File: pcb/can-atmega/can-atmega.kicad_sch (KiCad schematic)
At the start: 27 parts, among them J1 Screw_Terminal_01x02, J2 Screw_Terminal_01x02, J3 Conn_01x04_Female, J4 Conn_01x02_Female, J5 Conn_01x08_Female, U1 LM1117-5.0, U2 TJA1051T, U3 MCP2515-xSO, U4 ATmega328P-A, X1 16MHz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

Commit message: motor module
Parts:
- removed J4: Conn_01x02_Female, Connector_PinSocket_2.54mm:PinSocket_1x02_P2.54mm_Vertical, symbol Connector:Conn_01x02_Female
- removed J5: Conn_01x08_Female, Connector_PinSocket_2.54mm:PinSocket_1x08_P2.54mm_Vertical, symbol Connector:Conn_01x08_Female
- added J4: Connector_female, CAN_ATmega:Connector_female, symbol CAN_ATmega:Connector_female
- C1, C10, C11, C12, C3, C4, C5, C6, C7, C9: footprint Capacitor_SMD_Custom:C_KEM_0805_2.0x1.25mm -> Capacitor_SMD:C_1206_3216Metric
- C2, C8: footprint Capacitor_SMD_Custom:C_TAJ_3516_Bauform_A -> Capacitor_SMD:C_1206_3216Metric
- LED1: footprint LED_SMD_Custom:LED_EL_0603_GR1_1608 -> LED_SMD:LED_0805_2012Metric
- R1, R2, R3: footprint Resistors_SMD_Custom:R_SPR-0603_1.6x0.8mm -> Resistor_SMD:R_0805_2012Metric
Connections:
- net +5V: now also J4.2 (+5V)
- net GND: now also J4.3 (GND)
- net U4_A0: now also J4.8 (A0)
- net U4_A1: now also J4.9 (A1)
- net U4_A2: now also J4.10 (A2)
- net U4_A3: now also J4.11 (A3)
- net U4_D3: now also J4.4 (D3)
- net U4_D4: now also J4.5 (D4)
- net U4_D5: now also J4.6 (D5)
- net U4_D6: now also J4.7 (D6)
- net 12V renamed +12V
- net +12V: now also J4.1 (+12V)

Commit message: update pcb
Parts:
- J1, J2: footprint TerminalBlock:TerminalBlock_bornier-2_P5.08mm -> TerminalBlock_Phoenix:TerminalBlock_Phoenix_MKDS-1,5-2-5.08_1x02_P5.08mm_Horizontal
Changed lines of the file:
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@@
       (effects (font (size 1.27 1.27)) (justify left) hide)
     )
-    (property "Footprint" "TerminalBlock:TerminalBlock_bornier-2_P5.08mm" (id 2) (at 276.86 34.29 0)
+    (property "Footprint" "TerminalBlock_Phoenix:TerminalBlock_Phoenix_MKDS-1,5-2-5.08_1x02_P5.08mm_Horizontal" (id 2) (at 276.86 34.29 0)
       (effects (font (size 1.27 1.27)) hide)
     )
@@
       (effects (font (size 1.27 1.27)) (justify left) hide)
     )
-    (property "Footprint" "TerminalBlock:TerminalBlock_bornier-2_P5.08mm" (id 2) (at 24.13 31.75 0)
+    (property "Footprint" "TerminalBlock_Phoenix:TerminalBlock_Phoenix_MKDS-1,5-2-5.08_1x02_P5.08mm_Horizontal" (id 2) (at 24.13 31.75 0)
       (effects (font (size 1.27 1.27)) hide)
     )
@@
     )
     (path "/71aba0ac-da00-46fc-b041-6f563b5b4142"
-      (reference "J1") (unit 1) (value "Screw_Terminal_01x02") (footprint "TerminalBlock:TerminalBlock_bornier-2_P5.08mm")
+      (reference "J1") (unit 1) (value "Screw_Terminal_01x02") (footprint "TerminalBlock_Phoenix:TerminalBlock_Phoenix_MKDS-1,5-2-5.08_1x02_P5.08mm_Horizontal")
     )
     (path "/2120f6af-caaf-4baf-8a36-50ada20126a7"
-      (reference "J2") (unit 1) (value "Screw_Terminal_01x02") (footprint "TerminalBlock:TerminalBlock_bornier-2_P5.08mm")
+      (reference "J2") (unit 1) (value "Screw_Terminal_01x02") (footprint "TerminalBlock_Phoenix:TerminalBlock_Phoenix_MKDS-1,5-2-5.08_1x02_P5.08mm_Horizontal")
     )
     (path "/1e97e435-8faf-41d7-b7b1-5859024e8060"

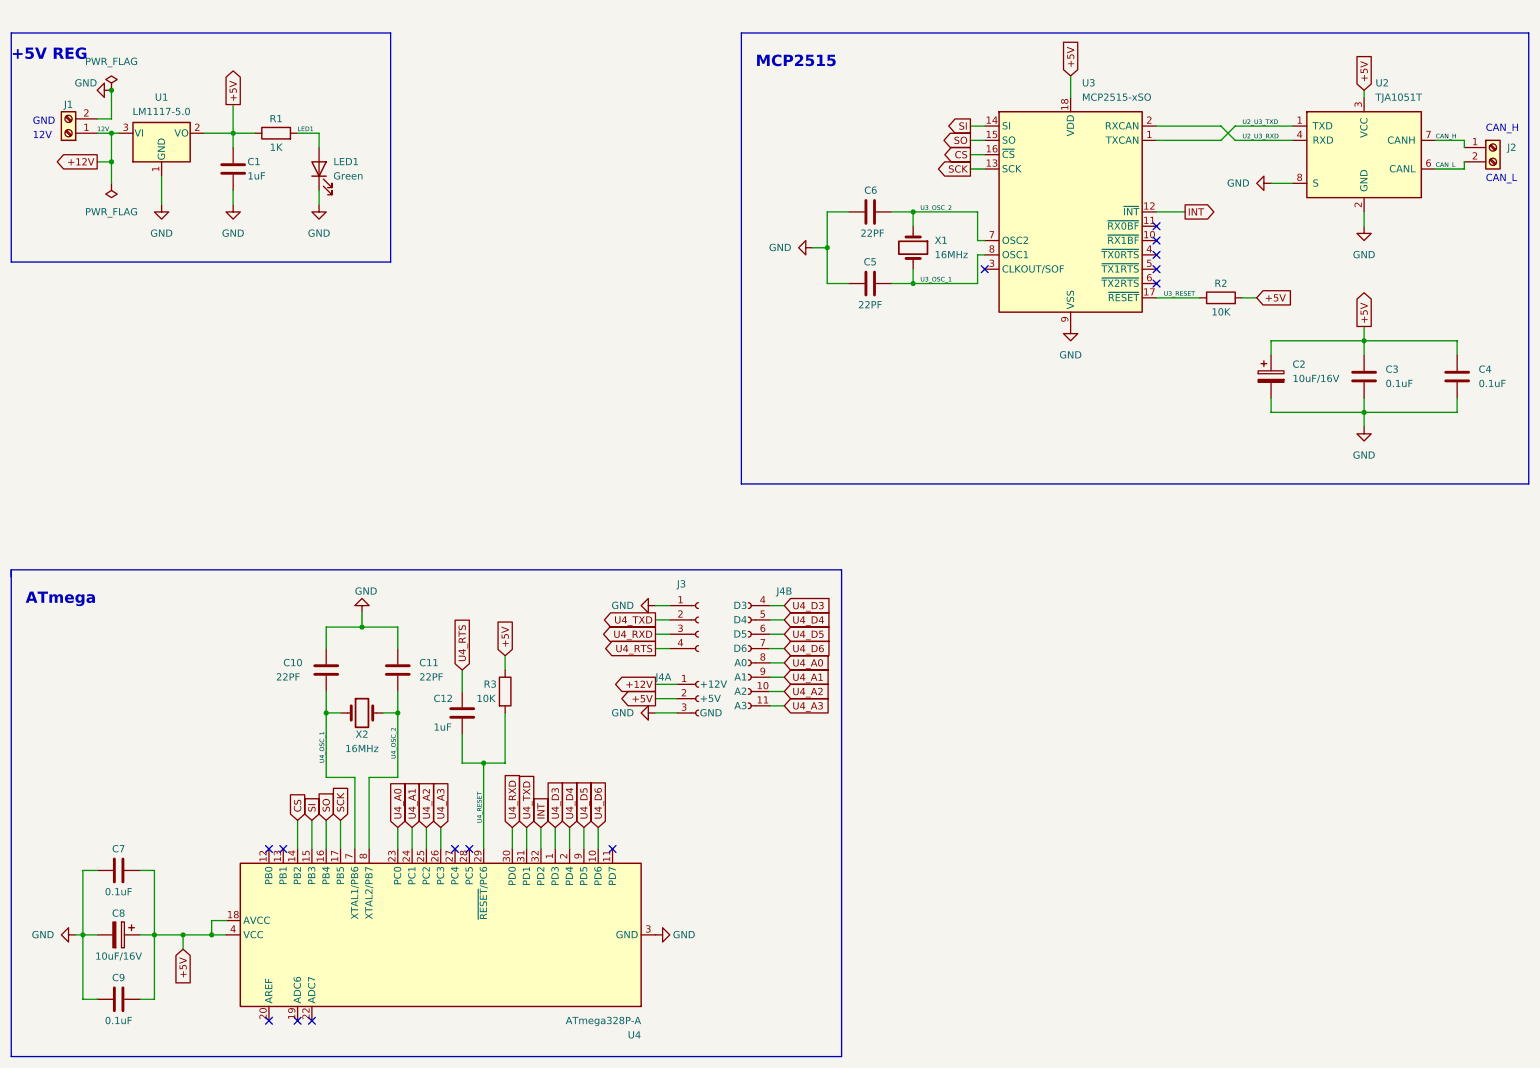
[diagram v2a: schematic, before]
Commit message: m12 plug; j1939 transition
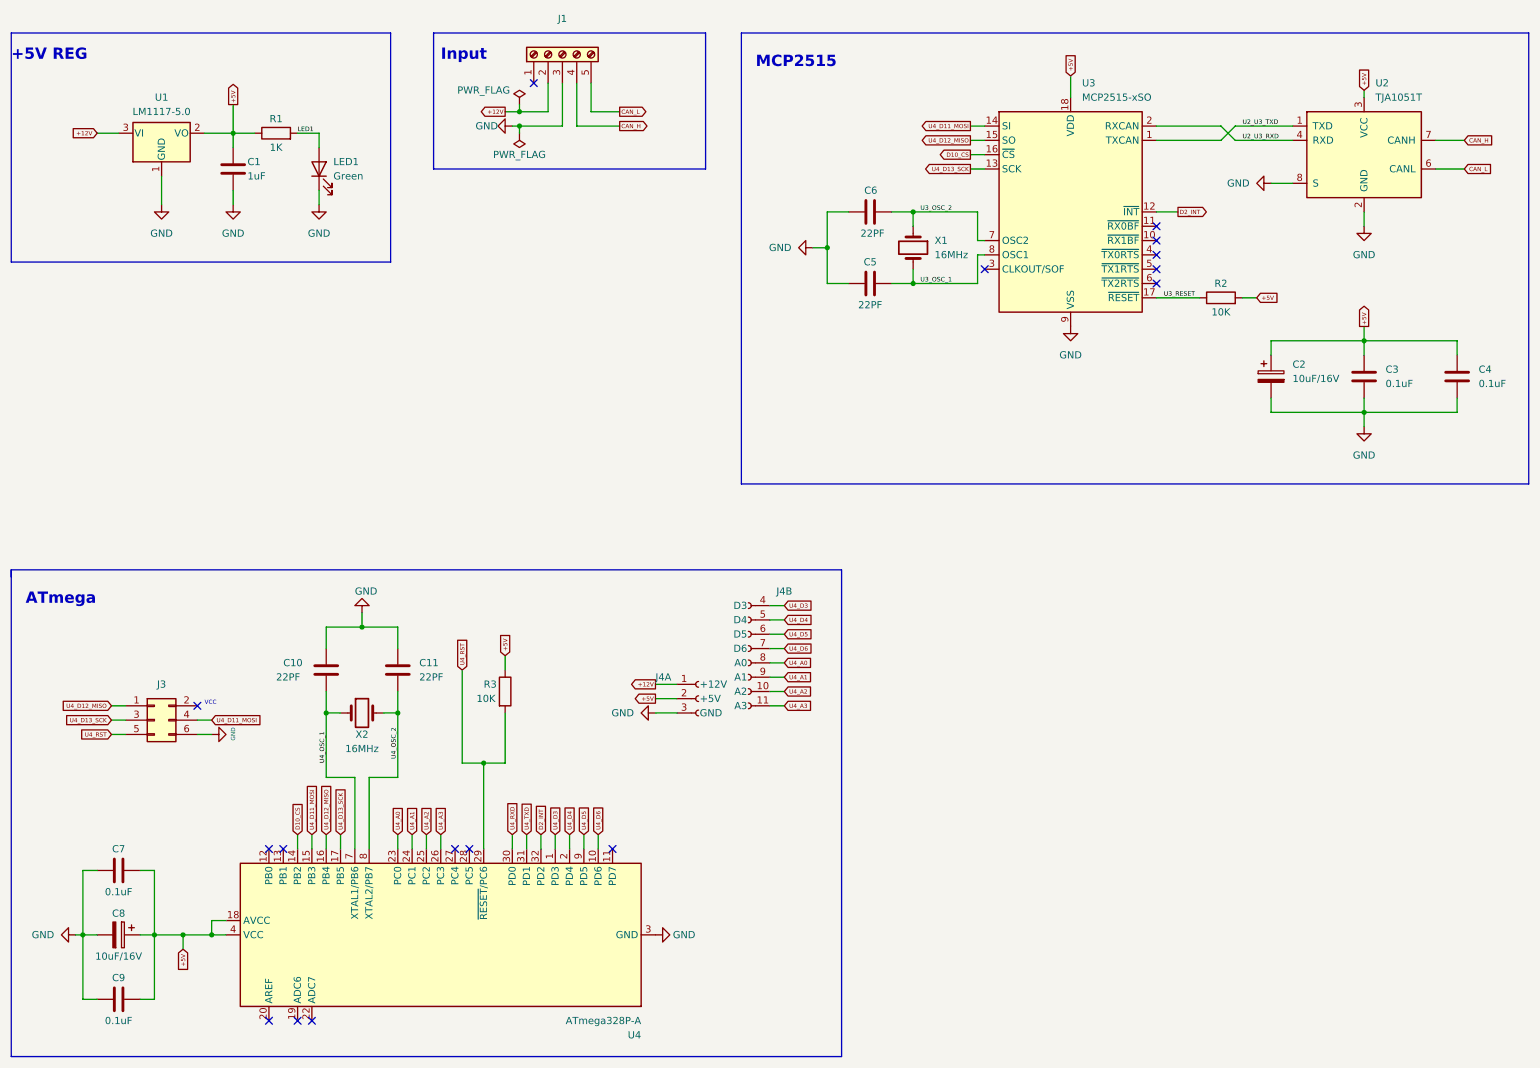
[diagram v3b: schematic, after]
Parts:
- removed C12: 1uF, Capacitor_SMD:C_1206_3216Metric, symbol Device:C
- removed J1, J2: Screw_Terminal_01x02, TerminalBlock_Phoenix:TerminalBlock_Phoenix_MKDS-1,5-2-5.08_1x02_P5.08mm_Horizontal, symbol Connector:Screw_Terminal_01x02
- removed J3: Conn_01x04_Female, Connector_PinSocket_2.54mm:PinSocket_1x04_P2.54mm_Vertical, symbol Connector:Conn_01x04_Female
- added J1: Screw_Terminal_01x05, mouser:4301207, symbol Connector:Screw_Terminal_01x05
- added J3: Conn_02x03_Odd_Even, Connector_IDC:IDC-Header_2x03_P2.54mm_Vertical, symbol Connector_Generic:Conn_02x03_Odd_Even
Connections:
- net +12V: now also J1.2 (Pin_2)
- net CAN_H: now also J1.4 (Pin_4)
- net CAN_L: now also J1.5 (Pin_5)
- net GND: now also J1.3 (Pin_3), J3.6 (Pin_6)
- net CS renamed D10_CS
- net INT renamed D2_INT
- net SCK renamed U4_D13_SCK
- net U4_D13_SCK: now also J3.3 (Pin_3)
- net SI renamed U4_D11_MOSI
- net U4_D11_MOSI: now also J3.4 (Pin_4)
- net SO renamed U4_D12_MISO
- net U4_D12_MISO: now also J3.1 (Pin_1)
- net U4_RESET renamed U4_RST
- net U4_RST: now also J3.5 (Pin_5)
- no-connect marks 14 -> 16
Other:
- note added: "Input"
- note added: "VCC"
- note removed: "12V"
- note removed: "CAN_H"
- note removed: "CAN_L"
- note removed: "GND"

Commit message: updated pcb
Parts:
- added L1: 10uH, Inductor_SMD:L_0805_2012Metric, symbol pspice:INDUCTOR
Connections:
- net +5V: now also L1.1; no longer U4.18 (AVCC)
- new net AVCC: L1.2, U4.18 (AVCC)
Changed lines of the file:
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@@
   (junction (at 97.79 143.51) (diameter 0) (color 0 0 0 0)
-  )
-  (junction (at 49.53 173.99) (diameter 0) (color 0 0 0 0)
   )
   (junction (at 173.99 45.72) (diameter 0) (color 0 0 0 0)
@@
     (stroke (width 0) (type default) (color 0 0 0 0))
   )
+  (wire (pts (xy 44.45 158.75) (xy 44.45 157.48))
+    (stroke (width 0) (type default) (color 0 0 0 0))
+  )
   (wire (pts (xy 186.69 53.34) (xy 185.42 53.34))
     (stroke (width 0) (type default) (color 0 0 0 0))
@@
     (stroke (width 0) (type default) (color 0 0 0 0))
   )
-  (wire (pts (xy 44.45 173.99) (xy 49.53 173.99))
-    (stroke (width 0) (type default) (color 0 0 0 0))
-  )
   (wire (pts (xy 228.6 33.02) (xy 217.17 33.02))
     (stroke (width 0) (type default) (color 0 0 0 0))
@@
     (stroke (width 0) (type default) (color 0 0 0 0))
   )
-  (wire (pts (xy 49.53 171.45) (xy 52.07 171.45))
-    (stroke (width 0) (type default) (color 0 0 0 0))
-  )
   (wire (pts (xy 254 66.04) (xy 254 68.58))
     (stroke (width 0) (type default) (color 0 0 0 0))
@@
     (stroke (width 0) (type default) (color 0 0 0 0))
   )
+  (wire (pts (xy 44.45 171.45) (xy 44.45 173.99))
+    (stroke (width 0) (type default) (color 0 0 0 0))
+  )
   (polyline (pts (xy 13.97 195.58) (xy 161.29 195.58))
     (stroke (width 0) (type default) (color 0 0 0 0))
@@
     (stroke (width 0) (type default) (color 0 0 0 0))
   )
-  (wire (pts (xy 49.53 173.99) (xy 52.07 173.99))
+  (wire (pts (xy 44.45 173.99) (xy 52.07 173.99))
     (stroke (width 0) (type default) (color 0 0 0 0))
   )
@@
     (stroke (width 0) (type default) (color 0 0 0 0))
   )
-  (wire (pts (xy 49.53 173.99) (xy 49.53 171.45))
-    (stroke (width 0) (type default) (color 0 0 0 0))
-  )
   (polyline (pts (xy 161.29 195.58) (xy 161.29 109.22))
     (stroke (width 0) (type default) (color 0 0 0 0))
@@
   )
   (wire (pts (xy 67.31 158.75) (xy 67.31 156.21))
+    (stroke (width 0) (type default) (color 0 0 0 0))
+  )
+  (wire (pts (xy 44.45 157.48) (xy 52.07 157.48))
+    (stroke (width 0) (type default) (color 0 0 0 0))
+  )
+  (wire (pts (xy 52.07 157.48) (xy 52.07 171.45))
     (stroke (width 0) (type default) (color 0 0 0 0))
   )
@@
   )
   (label "U4_OSC_1" (at 69.85 143.51 90)
+    (effects (font (size 0.8 0.8)) (justify left bottom))
+  )
+  (label "AVCC" (at 44.45 157.48 0)
     (effects (font (size 0.8 0.8)) (justify left bottom))
   )
@@
     )
     (property "Datasheet" "~" (id 3) (at 33.02 162.56 0)
+      (effects (font (size 1.27 1.27)) hide)
+    )
+    (pin "1")
+    (pin "2")
+  )
+  (symbol (lib_id "pspice:INDUCTOR") (at 44.45 165.1 90) (unit 1)
+    (in_bom yes) (on_board yes)
+    (property "Reference" "L1" (id 0) (at 44.45 164.465 90)
+      (effects (font (size 1.27 1.27)) (justify right))
+    )
+    (property "Value" "10uH" (id 1) (at 44.45 166.37 90)
+      (effects (font (size 1.27 1.27)) (justify right))
+    )
+    (property "Footprint" "Inductor_SMD:L_0805_2012Metric" (id 2) (at 44.45 165.1 0)
+      (effects (font (size 1.27 1.27)) hide)
+    )
+    (property "Datasheet" "~" (id 3) (at 44.45 165.1 0)
       (effects (font (size 1.27 1.27)) hide)
     )
@@
       (reference "J4") (unit 2) (value "Connector_female") (footprint "CAN_ATmega:Connector_female")
     )
+    (path "/239c80f6-4923-4337-bc99-824686c83a49"
+      (reference "L1") (unit 1) (value "10uH") (footprint "Inductor_SMD:L_0805_2012Metric")
+    )
     (path "/cb986dfa-de7c-4747-ad08-78d0c57370f5"

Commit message: pcb update
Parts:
- removed J4: Connector_female, CAN_ATmega:Connector_female, symbol CAN_ATmega:Connector_female
- added C10: 0.1uF, Capacitor_SMD:C_1206_3216Metric, symbol Device:C
- added J4: Connector_female_4x8, CAN_ATmega:Connector_female_4x8, symbol CAN_ATmega:Connector_female_4x8
- L1: footprint Inductor_SMD:L_0805_2012Metric -> Inductor_SMD:L_Neosid_SMS-ME3010
- LED1: footprint LED_SMD:LED_0805_2012Metric -> led_tube_MEN_12711000:led_tube_MEN_12711000
- renumbered C10 to C11, C11 to C12, C8 to C7, C9 to C8, C7 to C9
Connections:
- net +12V: now also J4.1 (+12V)
- net +5V: now also J4.2 (+5V); no longer C9.1
- net AVCC: now also C9.2, J4.3 (AVCC)
- net GND: now also C9.1, C10.1, J4.4 (GND); no longer C9.2
- net U4_A0: now also J4.9 (A0)
- net U4_A1: now also J4.10 (A1)
- net U4_A2: now also J4.11 (A2)
- net U4_A3: now also J4.12 (A3)
- net U4_D3: now also J4.5 (D3)
- net U4_D4: now also J4.6 (D4)
- net U4_D5: now also J4.7 (D5)
- net U4_D6: now also J4.8 (D6)
- net AREF: now reaches U4.20 (AREF)
- net AREF: now also C10.2
- no-connect marks 16 -> 15
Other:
- moved on the sheet: C11, C12, C7, C8, C9, J3, L1, R3, U4, X2

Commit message: pcb fab 2025-07-04
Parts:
- C2, C7: footprint Capacitor_SMD:C_1206_3216Metric -> Capacitor_Tantalum_SMD:CP_EIA-3216-18_Kemet-A
- LED1: footprint led_tube_MEN_12711000:led_tube_MEN_12711000 -> LED_SMD:LED_0805_2012Metric
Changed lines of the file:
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@@
     (property "Reference" "C7" (id 0) (at 24.13 169.545 0))
     (property "Value" "10uF/16V" (id 1) (at 20.32 171.45 0))
-    (property "Footprint" "Capacitor_SMD:C_1206_3216Metric" (id 2) (at 29.5402 173.99 0)
+    (property "Footprint" "Capacitor_Tantalum_SMD:CP_EIA-3216-18_Kemet-A" (id 2) (at 29.5402 173.99 0)
       (effects (font (size 1.27 1.27)) hide)
     )
@@
       (effects (font (size 1.27 1.27)) (justify left))
     )
-    (property "Footprint" "Capacitor_SMD:C_1206_3216Metric" (id 2) (at 238.4552 78.74 0)
+    (property "Footprint" "Capacitor_Tantalum_SMD:CP_EIA-3216-18_Kemet-A" (id 2) (at 238.4552 78.74 0)
       (effects (font (size 1.27 1.27)) hide)
     )
@@
       (effects (font (size 1.27 1.27)) (justify right))
     )
-    (property "Footprint" "led_tube_MEN_12711000:led_tube_MEN_12711000" (id 2) (at 68.58 38.1 0)
+    (property "Footprint" "LED_SMD:LED_0805_2012Metric" (id 2) (at 68.58 38.1 0)
       (effects (font (size 1.27 1.27)) hide)
     )
@@
     )
     (path "/bb2e7277-c4e4-4107-b435-483d93c0988e"
-      (reference "C2") (unit 1) (value "10uF/16V") (footprint "Capacitor_SMD:C_1206_3216Metric")
+      (reference "C2") (unit 1) (value "10uF/16V") (footprint "Capacitor_Tantalum_SMD:CP_EIA-3216-18_Kemet-A")
     )
     (path "/d3f71e8a-9a2f-4a97-9998-c927aa032ae4"
@@
     )
     (path "/3d9a1a36-2f4f-43b7-9e0d-58b9f0e71e07"
-      (reference "C7") (unit 1) (value "10uF/16V") (footprint "Capacitor_SMD:C_1206_3216Metric")
+      (reference "C7") (unit 1) (value "10uF/16V") (footprint "Capacitor_Tantalum_SMD:CP_EIA-3216-18_Kemet-A")
     )
     (path "/86084dcb-9556-40bb-a19f-7ff0d38f31a7"
@@
     )
     (path "/cb986dfa-de7c-4747-ad08-78d0c57370f5"
-      (reference "LED1") (unit 1) (value "Green") (footprint "led_tube_MEN_12711000:led_tube_MEN_12711000")
+      (reference "LED1") (unit 1) (value "Green") (footprint "LED_SMD:LED_0805_2012Metric")
     )
     (path "/8ef730e6-7745-407b-b999-e674f4f34f5f"
